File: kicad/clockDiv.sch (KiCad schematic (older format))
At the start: 2 parts

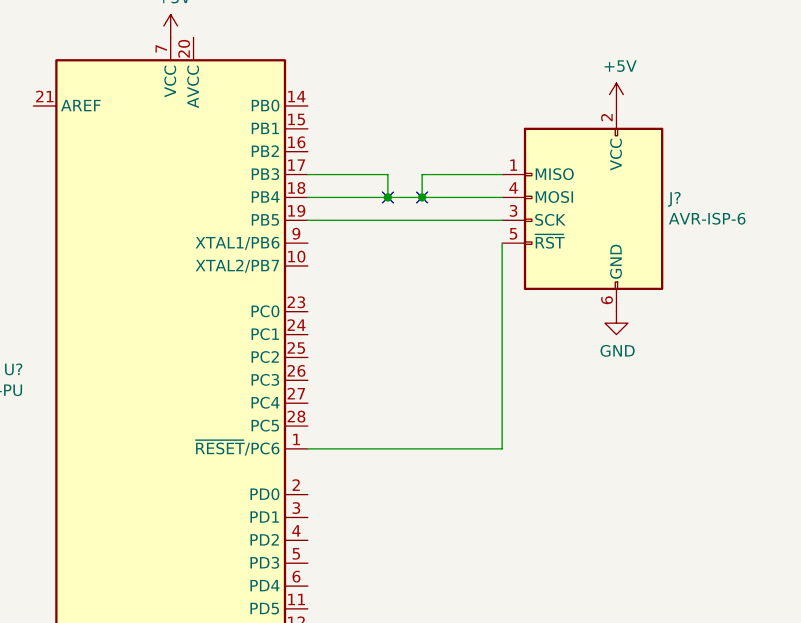
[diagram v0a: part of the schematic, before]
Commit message: replace crossing wires with labels
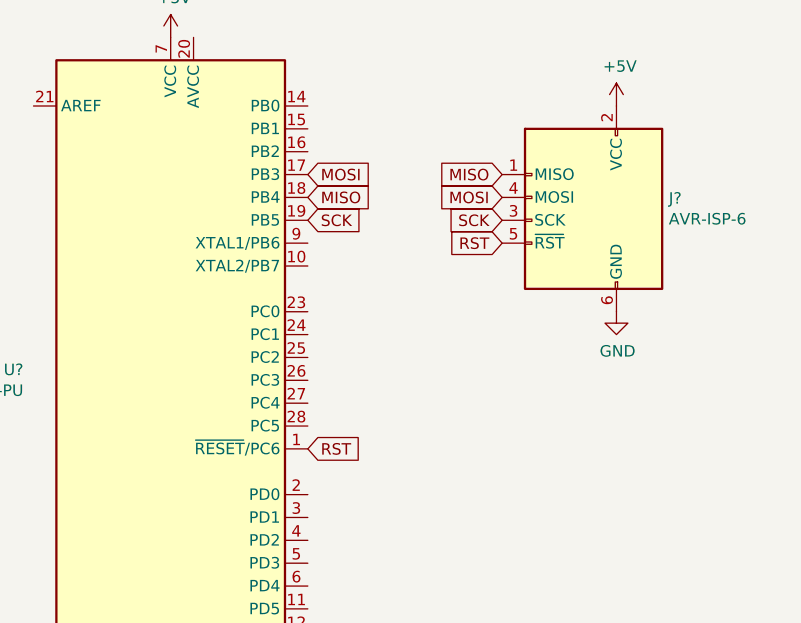
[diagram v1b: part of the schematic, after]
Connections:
- net RST: now reaches J?.5 (~RST), U?.1 (~RESET~/PC6)
- net MISO: now reaches J?.1 (MISO), U?.18 (PB4)
- net MISO: no longer J?.4 (MOSI), U?.17 (PB3)
- net SCK: now reaches J?.3 (SCK), U?.19 (PB5)
- new net MOSI: J?.4 (MOSI), U?.17 (PB3)
- no-connect marks 2 -> 0
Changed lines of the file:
@@
 	-1   0    0    -1
 $EndComp
-Wire Wire Line
-	6600 3100 5750 3100
-Wire Wire Line
-	6100 3000 6100 2900
-Wire Wire Line
-	6100 2900 5750 2900
-Wire Wire Line
-	6600 2900 6250 2900
-Wire Wire Line
-	6250 2900 6250 3000
-Wire Wire Line
-	5750 3000 6100 3000
-Connection ~ 6250 3000
-Wire Wire Line
-	6250 3000 6600 3000
-Connection ~ 6100 3000
-Wire Wire Line
-	6100 3000 6250 3000
-NoConn ~ 6250 3000
-NoConn ~ 6100 3000
-Wire Wire Line
-	6600 3200 6600 4100
-Wire Wire Line
-	6600 4100 5750 4100
 $Comp
 L power:GND #PWR?
@@
 	1    0    0    -1
 $EndComp
+Text GLabel 5750 3100 2    50   Input ~ 0
+SCK
+Text GLabel 6600 3100 0    50   Input ~ 0
+SCK
+Text GLabel 5750 3000 2    50   Input ~ 0
+MISO
+Text GLabel 6600 2900 0    50   Input ~ 0
+MISO
+Text GLabel 5750 2900 2    50   Input ~ 0
+MOSI
+Text GLabel 6600 3000 0    50   Input ~ 0
+MOSI
+Text GLabel 5750 4100 2    50   Input ~ 0
+RST
+Text GLabel 6600 3200 0    50   Input ~ 0
+RST
 $EndSCHEMATC

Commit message: add crystal
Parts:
- added Y?: Crystal 16MHz, symbol Device:Crystal
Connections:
- net at U?.10 (XTAL2/PB7): now also Y?.2
- net at U?.9 (XTAL1/PB6): now also Y?.1
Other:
- moved on the sheet: J?
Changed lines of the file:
@@
 L Connector:AVR-ISP-6 J?
 U 1 1 5EFE5F5A
-P 7000 3100
-F 0 "J?" H 6671 3196 50  0000 R CNN
-F 1 "AVR-ISP-6" H 6671 3105 50  0000 R CNN
-F 2 "" V 6750 3150 50  0001 C CNN
-F 3 " ~" H 5725 2550 50  0001 C CNN
-	1    7000 3100
+P 7350 3000
+F 0 "J?" H 7021 3096 50  0000 R CNN
+F 1 "AVR-ISP-6" H 7021 3005 50  0000 R CNN
+F 2 "" V 7100 3050 50  0001 C CNN
+F 3 " ~" H 6075 2450 50  0001 C CNN
+	1    7350 3000
 	-1   0    0    -1
 $EndComp
@@
 L power:GND #PWR?
 U 1 1 5EFF1BEB
-P 7100 3500
-F 0 "#PWR?" H 7100 3250 50  0001 C CNN
-F 1 "GND" H 7105 3327 50  0000 C CNN
-F 2 "" H 7100 3500 50  0001 C CNN
-F 3 "" H 7100 3500 50  0001 C CNN
-	1    7100 3500
+P 7450 3400
+F 0 "#PWR?" H 7450 3150 50  0001 C CNN
+F 1 "GND" H 7455 3227 50  0000 C CNN
+F 2 "" H 7450 3400 50  0001 C CNN
+F 3 "" H 7450 3400 50  0001 C CNN
+	1    7450 3400
 	1    0    0    -1
 $EndComp
@@
 L power:+5V #PWR?
 U 1 1 5EFF32A5
-P 7100 2600
-F 0 "#PWR?" H 7100 2450 50  0001 C CNN
-F 1 "+5V" H 7115 2773 50  0000 C CNN
-F 2 "" H 7100 2600 50  0001 C CNN
-F 3 "" H 7100 2600 50  0001 C CNN
-	1    7100 2600
+P 7450 2500
+F 0 "#PWR?" H 7450 2350 50  0001 C CNN
+F 1 "+5V" H 7465 2673 50  0000 C CNN
+F 2 "" H 7450 2500 50  0001 C CNN
+F 3 "" H 7450 2500 50  0001 C CNN
+	1    7450 2500
 	1    0    0    -1
 $EndComp
 Text GLabel 5750 3100 2    50   Input ~ 0
 SCK
-Text GLabel 6600 3100 0    50   Input ~ 0
+Text GLabel 6950 3000 0    50   Input ~ 0
 SCK
 Text GLabel 5750 3000 2    50   Input ~ 0
 MISO
-Text GLabel 6600 2900 0    50   Input ~ 0
+Text GLabel 6950 2800 0    50   Input ~ 0
 MISO
 Text GLabel 5750 2900 2    50   Input ~ 0
 MOSI
-Text GLabel 6600 3000 0    50   Input ~ 0
+Text GLabel 6950 2900 0    50   Input ~ 0
 MOSI
 Text GLabel 5750 4100 2    50   Input ~ 0
 RST
-Text GLabel 6600 3200 0    50   Input ~ 0
+Text GLabel 6950 3100 0    50   Input ~ 0
 RST
+$Comp
+L Device:Crystal Y?
+U 1 1 5EFE63D4
+P 6100 3350
+F 0 "Y?" V 6054 3481 50  0000 L CNN
+F 1 "Crystal 16MHz" V 6145 3481 50  0000 L CNN
+F 2 "" H 6100 3350 50  0001 C CNN
+F 3 "~" H 6100 3350 50  0001 C CNN
+	1    6100 3350
+	0    1    1    0
+$EndComp
+Wire Wire Line
+	6100 3200 5750 3200
+Wire Wire Line
+	6100 3500 5950 3500
+Wire Wire Line
+	5950 3500 5950 3300
+Wire Wire Line
+	5950 3300 5750 3300
 $EndSCHEMATC

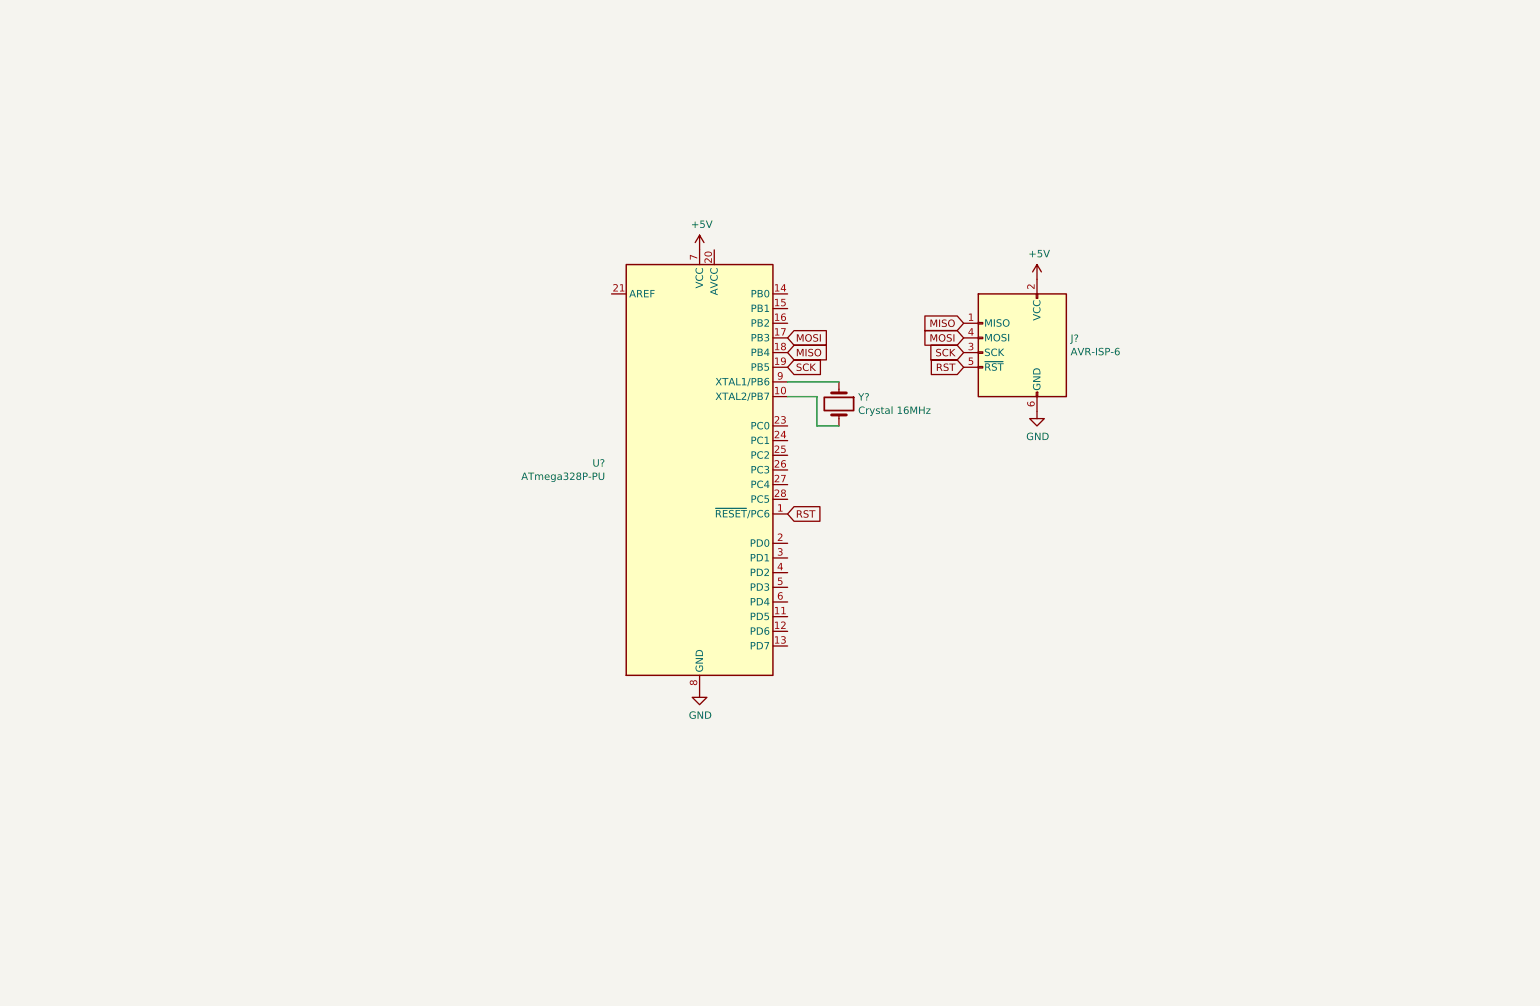
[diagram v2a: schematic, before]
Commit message: add labels for all divisions; add clock in circuit
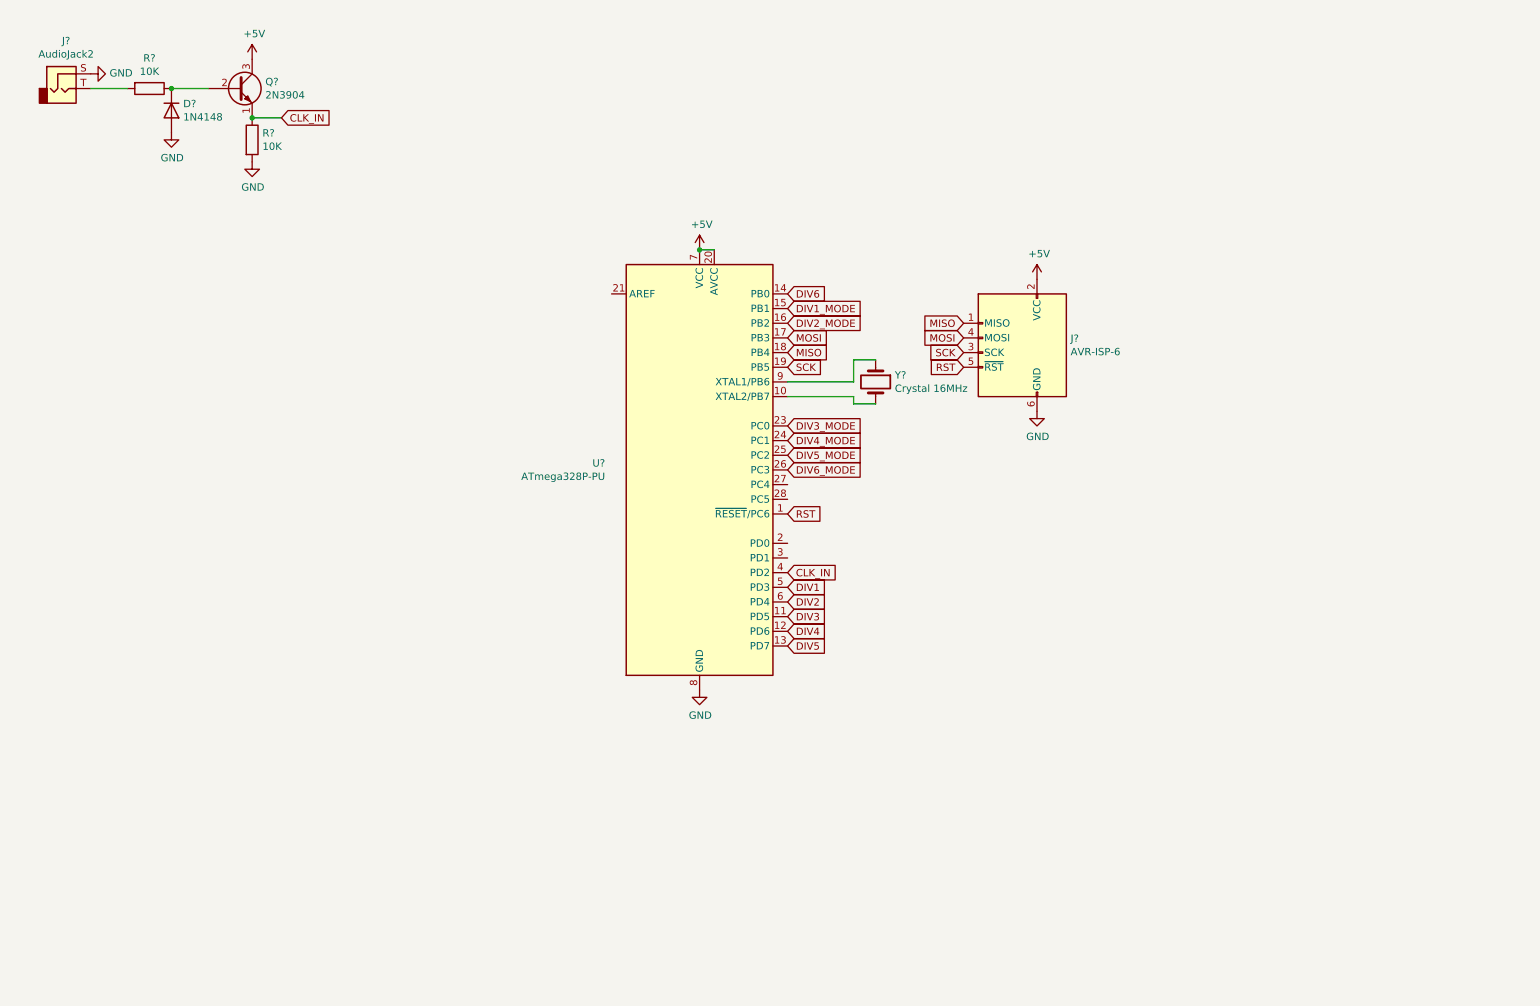
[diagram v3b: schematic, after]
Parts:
- added D?: 1N4148, Diode_THT:D_DO-35_SOD27_P7.62mm_Horizontal, symbol Diode:1N4148
- added J?: AudioJack2, symbol Connector:AudioJack2
- added Q?: 2N3904, Package_TO_SOT_THT:TO-92_Inline, symbol Transistor_BJT:2N3904
- added R? (x2): 10K, symbol Device:R
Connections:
- net +5V: now also U?.20 (AVCC), Q?.3 (C)
- net GND: now also D?.2 (A), J?.S, R?.2
- net DIV3: now reaches U?.11 (PD5)
- net DIV4: now reaches U?.12 (PD6)
- net DIV5: now reaches U?.13 (PD7)
- net DIV6: now reaches U?.14 (PB0)
- net DIV1_MODE: now reaches U?.15 (PB1)
- net DIV2_MODE: now reaches U?.16 (PB2)
- net DIV3_MODE: now reaches U?.23 (PC0)
- net DIV4_MODE: now reaches U?.24 (PC1)
- net DIV5_MODE: now reaches U?.25 (PC2)
- net DIV6_MODE: now reaches U?.26 (PC3)
- net CLK_IN: now reaches U?.4 (PD2)
- net CLK_IN: now also Q?.1 (E), R?.1
- net DIV1: now reaches U?.5 (PD3)
- net DIV2: now reaches U?.6 (PD4)
- new net: D?.1 (K), Q?.2 (B), R?.1
- new net: J?.T, R?.2
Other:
- moved on the sheet: Y?
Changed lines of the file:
@@
 L Device:Crystal Y?
 U 1 1 5EFE63D4
-P 6100 3350
-F 0 "Y?" V 6054 3481 50  0000 L CNN
-F 1 "Crystal 16MHz" V 6145 3481 50  0000 L CNN
-F 2 "" H 6100 3350 50  0001 C CNN
-F 3 "~" H 6100 3350 50  0001 C CNN
-	1    6100 3350
+P 6350 3200
+F 0 "Y?" V 6304 3331 50  0000 L CNN
+F 1 "Crystal 16MHz" V 6395 3331 50  0000 L CNN
+F 2 "" H 6350 3200 50  0001 C CNN
+F 3 "~" H 6350 3200 50  0001 C CNN
+	1    6350 3200
 	0    1    1    0
 $EndComp
+Text GLabel 5750 4500 2    50   Input ~ 0
+CLK_IN
+Text GLabel 5750 4600 2    50   Input ~ 0
+DIV1
+Text GLabel 5750 4700 2    50   Input ~ 0
+DIV2
+Text GLabel 5750 4800 2    50   Input ~ 0
+DIV3
+Text GLabel 5750 4900 2    50   Input ~ 0
+DIV4
+Text GLabel 5750 5000 2    50   Input ~ 0
+DIV5
+Text GLabel 5750 2600 2    50   Input ~ 0
+DIV6
+Text GLabel 5750 2700 2    50   Input ~ 0
+DIV1_MODE
+Text GLabel 5750 2800 2    50   Input ~ 0
+DIV2_MODE
+Text GLabel 5750 3500 2    50   Input ~ 0
+DIV3_MODE
+Text GLabel 5750 3700 2    50   Input ~ 0
+DIV5_MODE
+Text GLabel 5750 3800 2    50   Input ~ 0
+DIV6_MODE
+Text GLabel 5750 3600 2    50   Input ~ 0
+DIV4_MODE
 Wire Wire Line
-	6100 3200 5750 3200
+	6350 3050 6200 3050
 Wire Wire Line
-	6100 3500 5950 3500
+	6200 3050 6200 3200
 Wire Wire Line
-	5950 3500 5950 3300
+	6200 3200 5750 3200
 Wire Wire Line
-	5950 3300 5750 3300
+	6350 3350 6200 3350
+Wire Wire Line
+	6200 3350 6200 3300
+Wire Wire Line
+	6200 3300 5750 3300
+Wire Wire Line
+	5250 2300 5150 2300
+Connection ~ 5150 2300
+Text GLabel 2300 1400 2    50   Input ~ 0
+CLK_IN
+$Comp
+L Device:R R?
+U 1 1 5F004578
+P 1400 1200
+F 0 "R?" V 1193 1200 50  0000 C CNN
+F 1 "10K" V 1284 1200 50  0000 C CNN
+F 2 "" V 1330 1200 50  0001 C CNN
+F 3 "~" H 1400 1200 50  0001 C CNN
+	1    1400 1200
+	0    1    1    0
+$EndComp
+$Comp
+L Transistor_BJT:2N3904 Q?
+U 1 1 5F005064
+P 2000 1200
+F 0 "Q?" H 2190 1246 50  0000 L CNN
+F 1 "2N3904" H 2190 1155 50  0000 L CNN
+F 2 "Package_TO_SOT_THT:TO-92_Inline" H 2200 1125 50  0001 L CIN
+F 3 "https://www.fairchildsemi.com/datasheets/2N/2N3904.pdf" H 2000 1200 50  0001 L CNN
+	1    2000 1200
+	1    0    0    -1
+$EndComp
+$Comp
+L Diode:1N4148 D?
+U 1 1 5F005C2C
+P 1550 1350
+F 0 "D?" V 1504 1430 50  0000 L CNN
+F 1 "1N4148" V 1595 1430 50  0000 L CNN
+F 2 "Diode_THT:D_DO-35_SOD27_P7.62mm_Horizontal" H 1550 1175 50  0001 C CNN
+F 3 "https://assets.nexperia.com/documents/data-sheet/1N4148_1N4448.pdf" H 1550 1350 50  0001 C CNN
+	1    1550 1350
+	0    1    1    0
+$EndComp
+$Comp
+L power:+5V #PWR?
+U 1 1 5F00737D
+P 2100 1000
+F 0 "#PWR?" H 2100 850 50  0001 C CNN
+F 1 "+5V" H 2115 1173 50  0000 C CNN
+F 2 "" H 2100 1000 50  0001 C CNN
+F 3 "" H 2100 1000 50  0001 C CNN
+	1    2100 1000
+	1    0    0    -1
+$EndComp
+$Comp
+L Device:R R?
+U 1 1 5F007957
+P 2100 1550
+F 0 "R?" H 2170 1596 50  0000 L CNN
+F 1 "10K" H 2170 1505 50  0000 L CNN
+F 2 "" V 2030 1550 50  0001 C CNN
+F 3 "~" H 2100 1550 50  0001 C CNN
+	1    2100 1550
+	1    0    0    -1
+$EndComp
+Wire Wire Line
+	2100 1400 2300 1400
+Connection ~ 2100 1400
+$Comp
+L power:GND #PWR?
+U 1 1 5F00A598
+P 2100 1700
+F 0 "#PWR?" H 2100 1450 50  0001 C CNN
+F 1 "GND" H 2105 1527 50  0000 C CNN
+F 2 "" H 2100 1700 50  0001 C CNN
+F 3 "" H 2100 1700 50  0001 C CNN
+	1    2100 1700
+	1    0    0    -1
+$EndComp
+$Comp
+L power:GND #PWR?
+U 1 1 5F00A991
+P 1550 1500
+F 0 "#PWR?" H 1550 1250 50  0001 C CNN
+F 1 "GND" H 1555 1327 50  0000 C CNN
+F 2 "" H 1550 1500 50  0001 C CNN
+F 3 "" H 1550 1500 50  0001 C CNN
+	1    1550 1500
+	1    0    0    -1
+$EndComp
+Wire Wire Line
+	1800 1200 1550 1200
+Connection ~ 1550 1200
+$Comp
+L Connector:AudioJack2 J?
+U 1 1 5F00C56D
+P 800 1200
+F 0 "J?" H 832 1525 50  0000 C CNN
+F 1 "AudioJack2" H 832 1434 50  0000 C CNN
+F 2 "" H 800 1200 50  0001 C CNN
+F 3 "~" H 800 1200 50  0001 C CNN
+	1    800  1200
+	1    0    0    -1
+$EndComp
+$Comp
+L power:GND #PWR?
+U 1 1 5F00FC2B
+P 1000 1100
+F 0 "#PWR?" H 1000 850 50  0001 C CNN
+F 1 "GND" V 1005 972 50  0000 R CNN
+F 2 "" H 1000 1100 50  0001 C CNN
+F 3 "" H 1000 1100 50  0001 C CNN
+	1    1000 1100
+	0    -1   -1   0
+$EndComp
+Wire Wire Line
+	1000 1200 1250 1200
 $EndSCHEMATC
